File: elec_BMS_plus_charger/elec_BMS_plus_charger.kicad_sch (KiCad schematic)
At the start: 10 parts

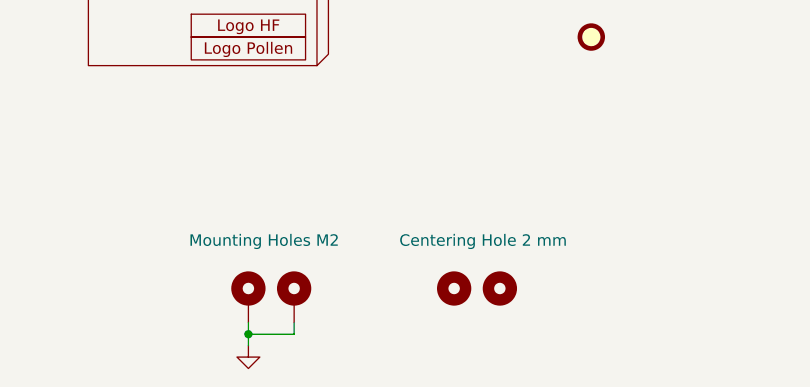
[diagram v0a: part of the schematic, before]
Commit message: [update] Mechanical adaptations.
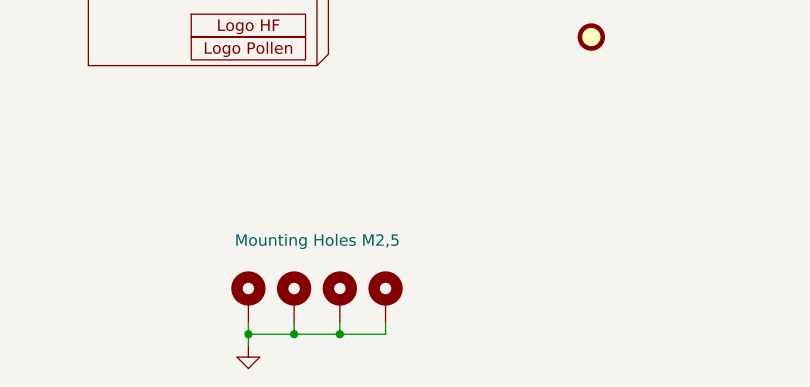
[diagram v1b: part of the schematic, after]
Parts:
- removed H6, H7: Centering Hole 2 mm, Library_Pollen:MountingHole_2.0mm, symbol Mechanical:MountingHole
- added H6, H7: Mounting Holes M2,5, MountingHole:MountingHole_2.7mm_M2.5_ISO7380_Pad_TopBottom, symbol Mechanical:MountingHole_Pad
- H4, H5: value Mounting Holes M2 -> Mounting Holes M2,5; footprint MountingHole:MountingHole_2.2mm_M2_ISO7380_Pad_TopBottom -> MountingHole:MountingHole_2.7mm_M2.5_ISO7380_Pad_TopBottom
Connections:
- net GND: now also H6.1, H7.1

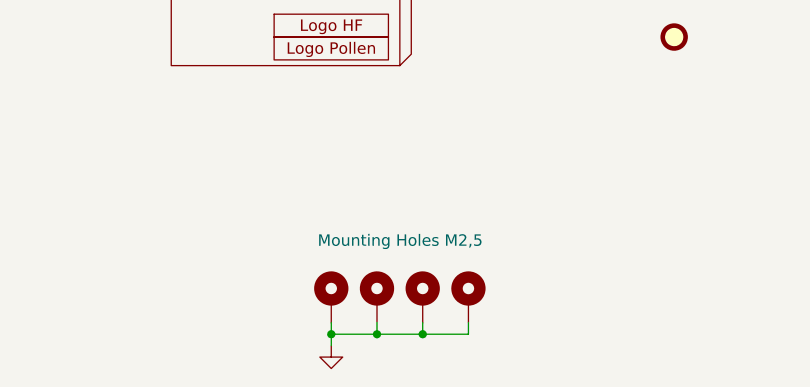
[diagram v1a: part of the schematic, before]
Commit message: [update] BMS+charger DRC OK
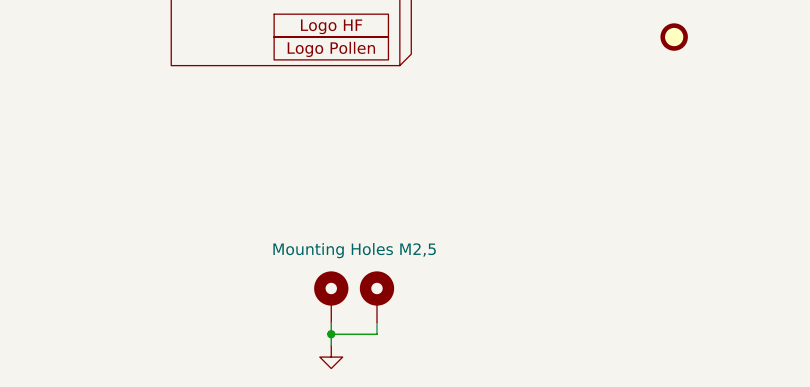
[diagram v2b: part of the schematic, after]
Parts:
- removed H6, H7: Mounting Holes M2,5, MountingHole:MountingHole_2.7mm_M2.5_ISO7380_Pad_TopBottom, symbol Mechanical:MountingHole_Pad
